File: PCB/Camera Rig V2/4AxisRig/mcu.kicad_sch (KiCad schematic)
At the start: 11 parts, among them SW1 SW_SPDT, SW2 SW_SPDT, U4 ESP32-S3-WROOM-1

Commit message: PCB V2 first draft
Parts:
- removed R20: 10k, Resistor_SMD:R_0603_1608Metric_Pad0.98x0.95mm_HandSolder, symbol Device:R_US
- removed SW1: SW_SPDT, symbol Switch:SW_SPDT
- added FB13: 2512065007Y6, Inductor_SMD:L_1206_3216Metric_Pad1.22x1.90mm_HandSolder, symbol Device:FerriteBead_Small
- added R44, R45: 4.7k, Resistor_SMD:R_0603_1608Metric_Pad0.98x0.95mm_HandSolder, symbol Device:R_US
- added SW1: PTS810SJS250SMTRLFS, PTS810SJS250SMTR:SMT_MTRLFS_CNK, symbol PTS810SJS250SMTR:PTS810SJS250SMTRLFS
- C24: renamed from C25; footprint (none) -> Capacitor_SMD:C_1206_3216Metric_Pad1.33x1.80mm_HandSolder
- C25: renamed from C24; footprint (none) -> Capacitor_SMD:C_0603_1608Metric_Pad1.08x0.95mm_HandSolder
- C26, C27: footprint (none) -> Capacitor_SMD:C_0603_1608Metric_Pad1.08x0.95mm_HandSolder
- SW2: footprint (none) -> SS-12D07-VG 4 NS GA PA:SS12D07_CNK; Unique FP y -> (none)
- U4: Unique FP y -> (none)
- renumbered R43 to R19, R44 to R20, R19 to R21
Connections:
- net 3V3: now also SW2.1 (A), FB13.1, R44.2, R45.2; no longer C24.1, C26.1, U4.2 (3V3)
- net DIAG1: now also U4.29 (IO36); no longer U4.6 (IO6)
- net DIAG2: now also U4.24 (IO47); no longer U4.18 (IO10)
- net DIAG3: now also U4.20 (IO12); no longer U4.22 (IO14)
- net DIR1: now also U4.26 (IO45); no longer U4.5 (IO5)
- net DIR2: now also U4.22 (IO14); no longer U4.17 (IO9)
- net DIR3: now also U4.18 (IO10); no longer U4.21 (IO13)
- net EN: now also C27.1, SW1.1, SW1.2; no longer C27.2, U4.9 (IO16)
- net ENC_A: now also U4.7 (IO7); no longer U4.26 (IO45)
- net ENC_B: now also U4.5 (IO5); no longer U4.24 (IO47)
- net ENC_C: now also U4.6 (IO6); no longer U4.16 (IO46)
- net EN_12V: now also U4.33 (IO40); no longer U4.32 (IO39)
- net FOCUS: now also U4.9 (IO16); no longer U4.35 (IO42)
- net GND: now also C27.2, SW1.3, SW1.4; no longer C27.1
- net I2C_SCL: now also R44.1
- net I2C_SDA: now also R45.1
- net SHUTTER: now also U4.8 (IO15); no longer U4.34 (IO41)
- net SPREAD: now also U4.15 (IO3); no longer U4.25 (IO48)
- net STDBY1: now also U4.25 (IO48); no longer U4.7 (IO7)
- net STDBY2: now also U4.21 (IO13); no longer U4.19 (IO11)
- net STDBY3: now also U4.17 (IO9); no longer U4.8 (IO15)
- net STEP1: now also U4.28 (IO35); no longer U4.4 (IO4)
- net STEP2: now also U4.23 (IO21); no longer U4.12 (IO8)
- net STEP3: now also U4.19 (IO11); no longer U4.20 (IO12)
- net SW: now also U4.4 (IO4); no longer U4.33 (IO40)
- net at R19.1, R20.2: now also U4.34 (IO41); no longer U4.15 (IO3)
- new net: C24.1, C26.1, FB13.2, U4.2 (3V3)
- new net EN_DRIVERS: U4.16 (IO46)
- no-connect marks 9 -> 2
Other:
- note added: "HIGH: Boot from flash LOW: Wait for USB"
- note added: "Press to reset"
- moved on the sheet: C24, C25, C26, R19, R20, R21, SW2

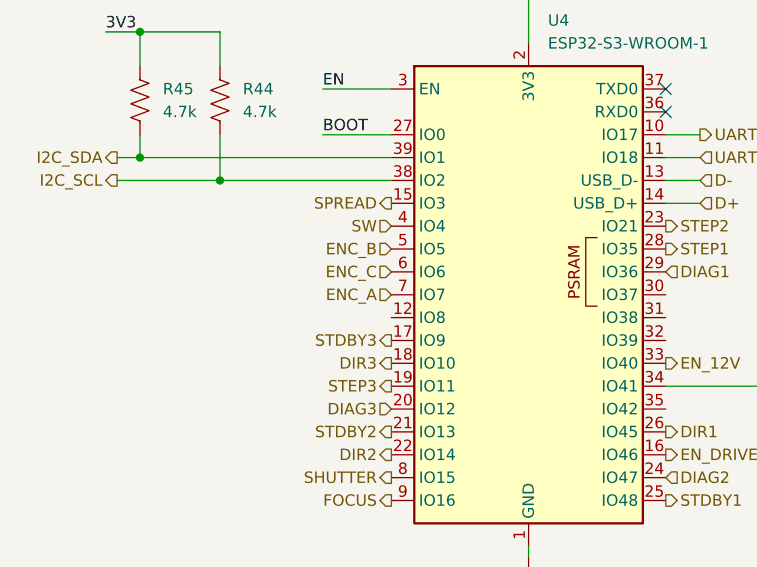
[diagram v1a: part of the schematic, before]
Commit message: Updated rotary encoder wiring
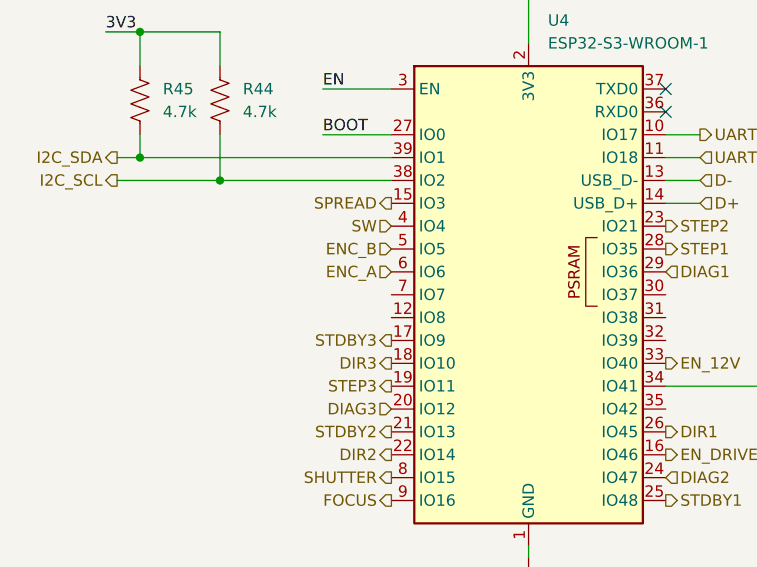
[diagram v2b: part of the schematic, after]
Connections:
- net ENC_C is gone; now on net ENC_A: U4.6 (IO6)
- net ENC_A: no longer U4.7 (IO7)
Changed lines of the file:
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@@
+		)
+	)
+	(hierarchical_label "D+"
+		(shape input)
+		(at 105.41 83.82 0)
+		(effects
+			(font
+				(size 1.27 1.27)
+			)
+			(justify left)
+		)
+	)
+	(hierarchical_label "STDBY2"
+		(shape output)
+		(at 71.12 109.22 180)
+		(effects
+			(font
+				(size 1.27 1.27)
+			)
+			(justify right)
+		)
+	)
+	(hierarchical_label "ENC_B"
+		(shape input)
+		(at 71.12 88.9 180)
+		(effects
+			(font
+				(size 1.27 1.27)
+			)
+			(justify right)
+		)
+	)
+	(hierarchical_label "SENSE_15V"
+		(shape input)
+		(at 129.54 92.71 180)
+		(effects
+			(font
+				(size 1.27 1.27)
+			)
+			(justify right)
+		)
+	)
+	(hierarchical_label "D-"
+		(shape input)
+		(at 105.41 81.28 0)
+		(effects
+			(font
+				(size 1.27 1.27)
+			)
+			(justify left)
+		)
+	)
+	(hierarchical_label "STDBY1"
+		(shape output)
+		(at 101.6 116.84 0)
+		(effects
+			(font
+				(size 1.27 1.27)
+			)
+			(justify left)
+		)
+	)
+	(hierarchical_label "SPREAD"
+		(shape output)
+		(at 71.12 83.82 180)
+		(effects
+			(font
+				(size 1.27 1.27)
+			)
+			(justify right)
+		)
+	)
+	(hierarchical_label "STEP2"
+		(shape output)
+		(at 101.6 86.36 0)
+		(effects
+			(font
+				(size 1.27 1.27)
+			)
+			(justify left)
+		)
+	)
+	(hierarchical_label "DIR2"
+		(shape output)
+		(at 71.12 111.76 180)
+		(effects
+			(font
+				(size 1.27 1.27)
+			)
+			(justify right)
+		)
+	)
+	(hierarchical_label "3V3"
+		(shape input)
+		(at 52.07 49.53 180)
+		(effects
+			(font
+				(size 1.27 1.27)
+			)
+			(justify right)
+		)
+	)
+	(hierarchical_label "STEP3"
+		(shape output)
+		(at 71.12 104.14 180)
+		(effects
+			(font
+				(size 1.27 1.27)
+			)
+			(justify right)
+		)
+	)
+	(hierarchical_label "EN_DRIVERS"
+		(shape output)
+		(at 101.6 111.76 0)
+		(effects
+			(font
+				(size 1.27 1.27)
+			)
+			(justify left)
+		)
+	)
+	(hierarchical_label "SHUTTER"
+		(shape output)
+		(at 71.12 114.3 180)
+		(effects
+			(font
+				(size 1.27 1.27)
+			)
+			(justify right)
+		)
+	)
+	(hierarchical_label "DIR3"
+		(shape output)
+		(at 71.12 101.6 180)
+		(effects
+			(font
+				(size 1.27 1.27)
+			)
+			(justify right)
+		)
+	)
+	(hierarchical_label "DIR1"
+		(shape output)
+		(at 101.6 109.22 0)
+		(effects
+			(font
+				(size 1.27 1.27)
+			)
+			(justify left)
+		)
+	)
+	(hierarchical_label "DIAG3"
+		(shape input)
+		(at 71.12 106.68 180)
+		(effects
+			(font
+				(size 1.27 1.27)
+			)
+			(justify right)
+		)
+	)
+	(hierarchical_label "I2C_SCL"
+		(shape output)
+		(at 40.64 81.28 180)
+		(effects
+			(font
+				(size 1.27 1.27)
+			)
+			(justify right)
+		)
+	)
+	(hierarchical_label "FOCUS"
+		(shape output)
+		(at 71.12 116.84 180)
+		(effects
+			(font
+				(size 1.27 1.27)
+			)
+			(justify right)
+		)
+	)
+	(hierarchical_label "STEP1"
+		(shape output)
+		(at 101.6 88.9 0)
+		(effects
+			(font
+				(size 1.27 1.27)
+			)
+			(justify left)
+		)
+	)
+	(hierarchical_label "UART_TX"
+		(shape output)
+		(at 105.41 76.2 0)
+		(effects
+			(font
+				(size 1.27 1.27)
+			)
+			(justify left)
+		)
+	)
+	(hierarchical_label "DIAG1"
+		(shape input)
+		(at 101.6 91.44 0)
+		(effects
+			(font
+				(size 1.27 1.27)
+			)
+			(justify left)
+		)
+	)
+	(hierarchical_label "I2C_SDA"
+		(shape output)
+		(at 40.64 78.74 180)
+		(effects
+			(font
+				(size 1.27 1.27)
+			)
+			(justify right)
+		)
+	)
+	(hierarchical_label "EN_12V"
+		(shape output)
+		(at 101.6 101.6 0)
+		(effects
+			(font
+				(size 1.27 1.27)
+			)
+			(justify left)
 		)
 	)
 	(hierarchical_label "ENC_A"
 		(shape input)
-		(at 71.12 93.98 180)
-		(effects
-			(font
-				(size 1.27 1.27)
-			)
-			(justify right)
-		)
-	)
-	(hierarchical_label "D+"
-		(shape input)
-		(at 105.41 83.82 0)
-		(effects
-			(font
-				(size 1.27 1.27)
-			)
-			(justify left)
-		)
-	)
-	(hierarchical_label "STDBY2"
-		(shape output)
-		(at 71.12 109.22 180)
-		(effects
-			(font
-				(size 1.27 1.27)
-			)
-			(justify right)
-		)
-	)
-	(hierarchical_label "SENSE_15V"
-		(shape input)
-		(at 129.54 92.71 180)
-		(effects
-			(font
-				(size 1.27 1.27)
-			)
-			(justify right)
-		)
-	)
-	(hierarchical_label "D-"
-		(shape input)
-		(at 105.41 81.28 0)
-		(effects
-			(font
-				(size 1.27 1.27)
-			)
-			(justify left)
-		)
-	)
-	(hierarchical_label "STDBY1"
-		(shape output)
-		(at 101.6 116.84 0)
-		(effects
-			(font
-				(size 1.27 1.27)
-			)
-			(justify left)
-		)
-	)
-	(hierarchical_label "SPREAD"
-		(shape output)
-		(at 71.12 83.82 180)
-		(effects
-			(font
-				(size 1.27 1.27)
-			)
-			(justify right)
-		)
-	)
-	(hierarchical_label "ENC_B"
-		(shape input)
-		(at 71.12 88.9 180)
-		(effects
-			(font
-				(size 1.27 1.27)
-			)
-			(justify right)
-		)
-	)
-	(hierarchical_label "STEP2"
-		(shape output)
-		(at 101.6 86.36 0)
-		(effects
-			(font
-				(size 1.27 1.27)
-			)
-			(justify left)
-		)
-	)
-	(hierarchical_label "DIR2"
-		(shape output)
-		(at 71.12 111.76 180)
-		(effects
-			(font
-				(size 1.27 1.27)
-			)
-			(justify right)
-		)
-	)
-	(hierarchical_label "ENC_C"
-		(shape input)
 		(at 71.12 91.44 180)
 		(effects
@@
 		)
 	)
-	(hierarchical_label "3V3"
-		(shape input)
-		(at 52.07 49.53 180)
-		(effects
-			(font
-				(size 1.27 1.27)
-			)
-			(justify right)
-		)
-	)
-	(hierarchical_label "STEP3"
-		(shape output)
-		(at 71.12 104.14 180)
-		(effects
-			(font
-				(size 1.27 1.27)
-			)
-			(justify right)
-		)
-	)
-	(hierarchical_label "EN_DRIVERS"
-		(shape output)
-		(at 101.6 111.76 0)
-		(effects
-			(font
-				(size 1.27 1.27)
-			)
-			(justify left)
-		)
-	)
-	(hierarchical_label "SHUTTER"
-		(shape output)
-		(at 71.12 114.3 180)
-		(effects
-			(font
-				(size 1.27 1.27)
-			)
-			(justify right)
-		)
-	)
-	(hierarchical_label "DIR3"
-		(shape output)
-		(at 71.12 101.6 180)
-		(effects
-			(font
-				(size 1.27 1.27)
-			)
-			(justify right)
-		)
-	)
-	(hierarchical_label "DIR1"
-		(shape output)
-		(at 101.6 109.22 0)
-		(effects
-			(font
-				(size 1.27 1.27)
-			)
-			(justify left)
-		)
-	)
-	(hierarchical_label "DIAG3"
-		(shape input)
-		(at 71.12 106.68 180)
-		(effects
-			(font
-				(size 1.27 1.27)
-			)
-			(justify right)
-		)
-	)
-	(hierarchical_label "I2C_SCL"
-		(shape output)
-		(at 40.64 81.28 180)
-		(effects
-			(font
-				(size 1.27 1.27)
-			)
-			(justify right)
-		)
-	)
-	(hierarchical_label "FOCUS"
-		(shape output)
-		(at 71.12 116.84 180)
-		(effects
-			(font
-				(size 1.27 1.27)
-			)
-			(justify right)
-		)
-	)
-	(hierarchical_label "STEP1"
-		(shape output)
-		(at 101.6 88.9 0)
-		(effects
-			(font
-				(size 1.27 1.27)
-			)
-			(justify left)
-		)
-	)
-	(hierarchical_label "UART_TX"
-		(shape output)
-		(at 105.41 76.2 0)
-		(effects
-			(font
-				(size 1.27 1.27)
-			)
-			(justify left)
-		)
-	)
-	(hierarchical_label "DIAG1"
-		(shape input)
-		(at 101.6 91.44 0)
-		(effects
-			(font
-				(size 1.27 1.27)
-			)
-			(justify left)
-		)
-	)
-	(hierarchical_label "I2C_SDA"
-		(shape output)
-		(at 40.64 78.74 180)
-		(effects
-			(font
-				(size 1.27 1.27)
-			)
-			(justify right)
-		)
-	)
-	(hierarchical_label "EN_12V"
-		(shape output)
-		(at 101.6 101.6 0)
-		(effects
-			(font
-				(size 1.27 1.27)
-			)
-			(justify left)
-		)
-	)

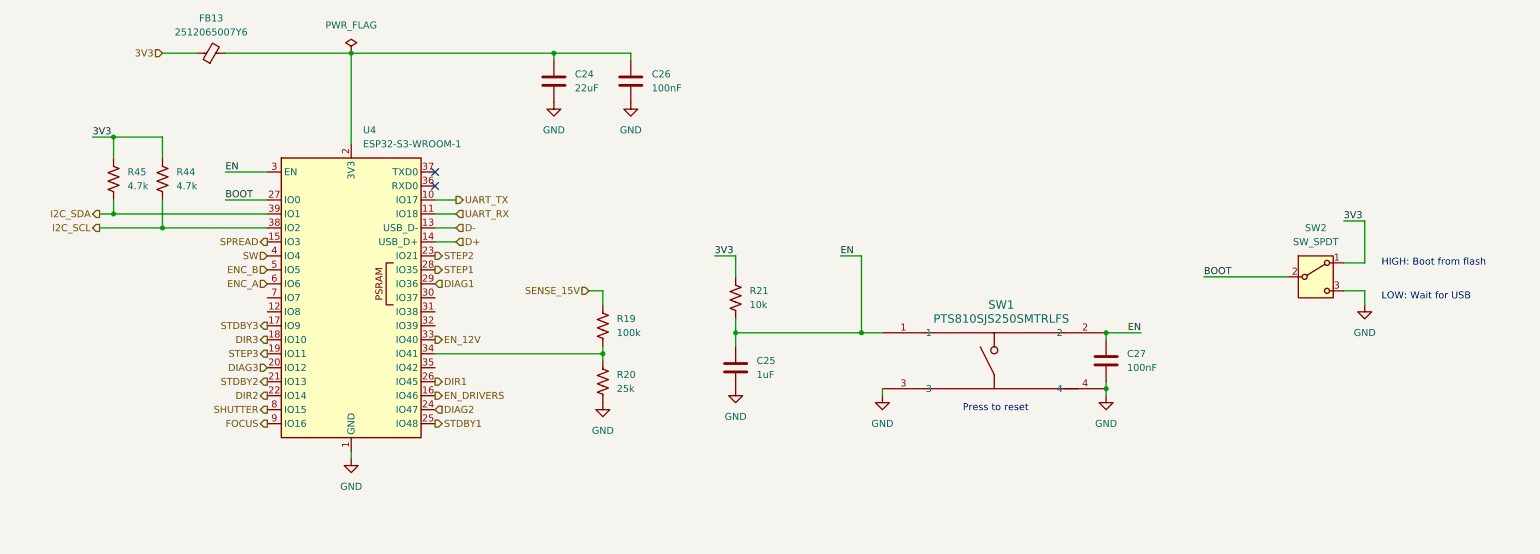
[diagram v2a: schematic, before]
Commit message: Netclass Improvements
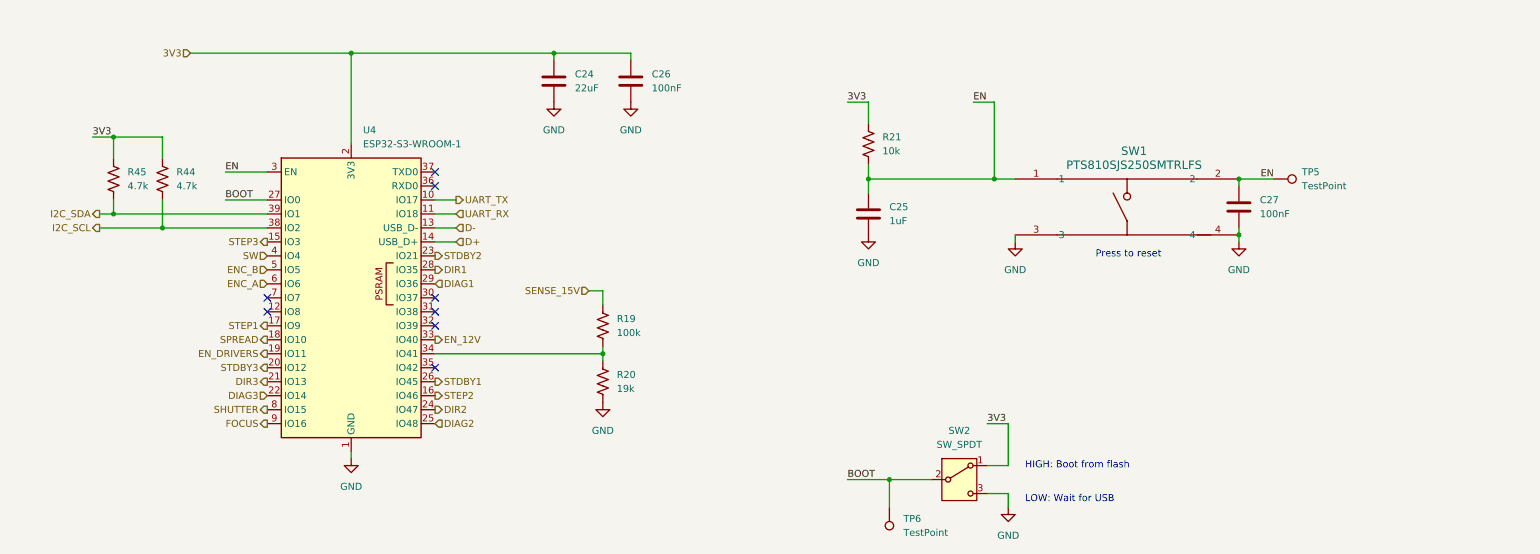
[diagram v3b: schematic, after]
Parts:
- removed FB13: 2512065007Y6, Inductor_SMD:L_1206_3216Metric_Pad1.22x1.90mm_HandSolder, symbol Device:FerriteBead_Small
- added TP5, TP6: TestPoint, TestPoint:TestPoint_Pad_1.0x1.0mm, symbol Connector:TestPoint
- R20: value 25k -> 19k
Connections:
- net 3V3: now also C24.1, C26.1, U4.2 (3V3)
- net BOOT: now also TP6.1
- net DIAG2: now also U4.25 (IO48); no longer U4.24 (IO47)
- net DIAG3: now also U4.22 (IO14); no longer U4.20 (IO12)
- net DIR1: now also U4.28 (IO35); no longer U4.26 (IO45)
- net DIR2: now also U4.24 (IO47); no longer U4.22 (IO14)
- net DIR3: now also U4.21 (IO13); no longer U4.18 (IO10)
- net EN: now also TP5.1
- net EN_DRIVERS: now also U4.19 (IO11); no longer U4.16 (IO46)
- net SPREAD: now also U4.18 (IO10); no longer U4.15 (IO3)
- net STDBY1: now also U4.26 (IO45); no longer U4.25 (IO48)
- net STDBY2: now also U4.23 (IO21); no longer U4.21 (IO13)
- net STDBY3: now also U4.20 (IO12); no longer U4.17 (IO9)
- net STEP1: now also U4.17 (IO9); no longer U4.28 (IO35)
- net STEP2: now also U4.16 (IO46); no longer U4.23 (IO21)
- net STEP3: now also U4.15 (IO3); no longer U4.19 (IO11)
- no-connect marks 2 -> 8
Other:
- moved on the sheet: C25, C27, R21, SW1, SW2
